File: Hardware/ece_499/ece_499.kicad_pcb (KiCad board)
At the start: 2 copper layers, 110.8 x 70 mm, 63 parts, among them J1 Conn_01x04, J2 Conn_01x04, J3 Conn_01x04, J4 Conn_01x04, J5 Conn_01x04, Q1 DMN2004WK, Q2 DMN2004WK, Q3 DMN2004WK, Q4 DMN2004WK, SW1 Encoder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

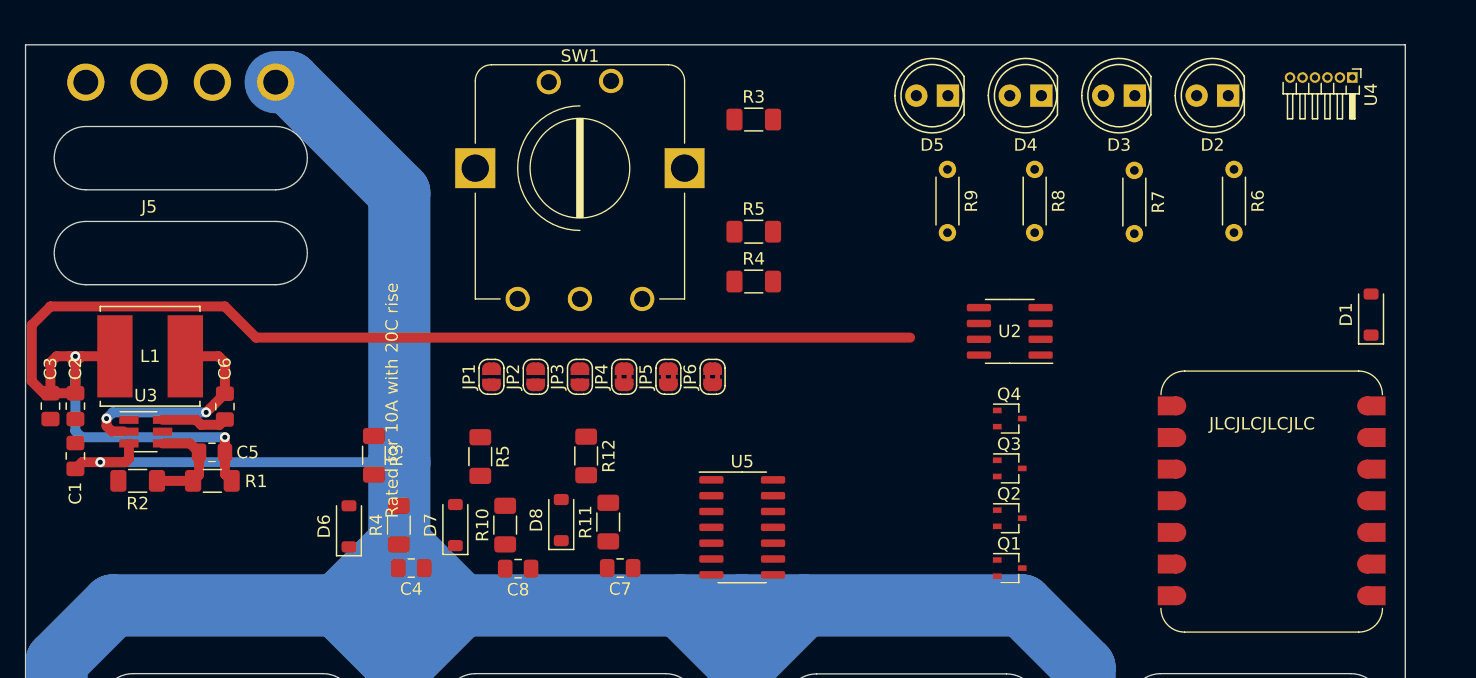
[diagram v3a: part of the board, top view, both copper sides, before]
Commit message: Implement 3v3 lines on PCB
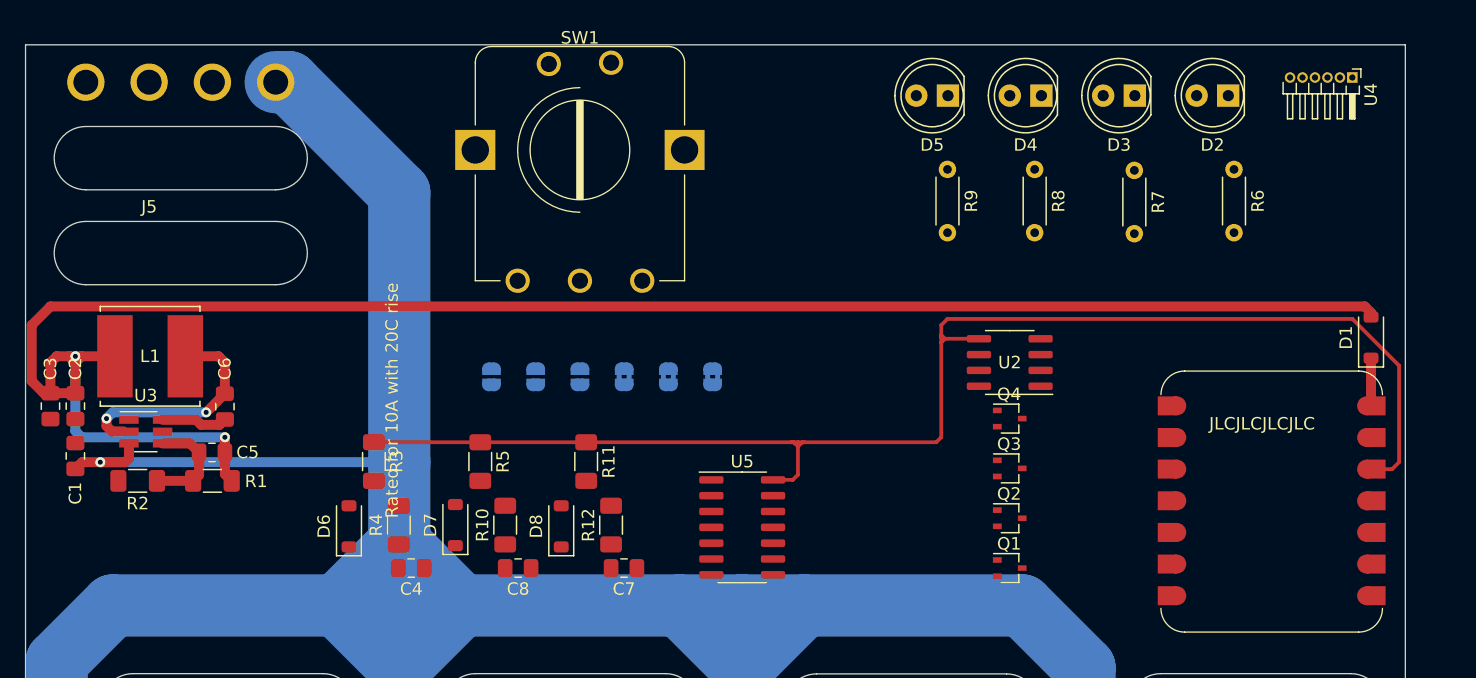
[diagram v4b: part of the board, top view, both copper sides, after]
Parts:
- removed the R3 at (158.4, 36.0)
- removed the R4 at (158.4, 49.0)
- removed the R5 at (158.4, 45.0)
- JP1, JP2, JP3, JP4, JP5, JP6: moved to B.Cu
- moved R12 5.90 mm to (147.0, 68.5), turned to 90 degrees
- moved R11 5.17 mm to (145.0, 63.5), turned to -90 degrees
- moved U2 2.50 mm to (179.0, 55.5)
- moved D1 1.85 mm to (208.0, 53.5)
- moved SW1 1.46 mm to (144.5, 48.9)
- moved D8 0.50 mm to (143.0, 68.7)
- moved R3 0.50 mm to (128.0, 63.5)
- moved R5 0.40 mm to (136.5, 63.5)
- moved C7 0.31 mm to (148.0, 72.0)
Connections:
- U1 pad 10: +3.3V -> +3V3
- U2 pad 5: +3.3V -> +3V3
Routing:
- net +3V3: track 0.00 -> 113.0 mm
- net +5V: track 114.7 -> 151.2 mm
- net Net-(D1-K): track 0.00 -> 4.00 mm

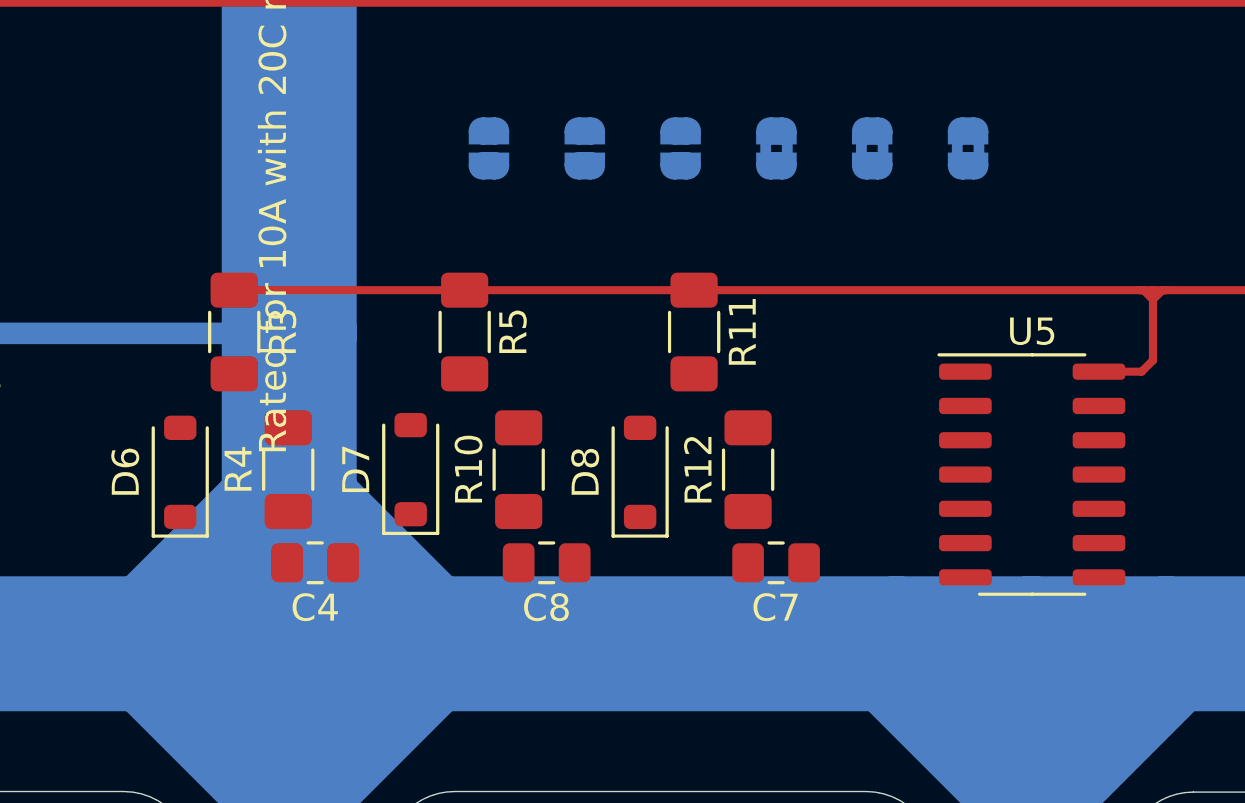
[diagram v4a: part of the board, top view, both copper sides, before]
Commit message: Implement encoder debouncer
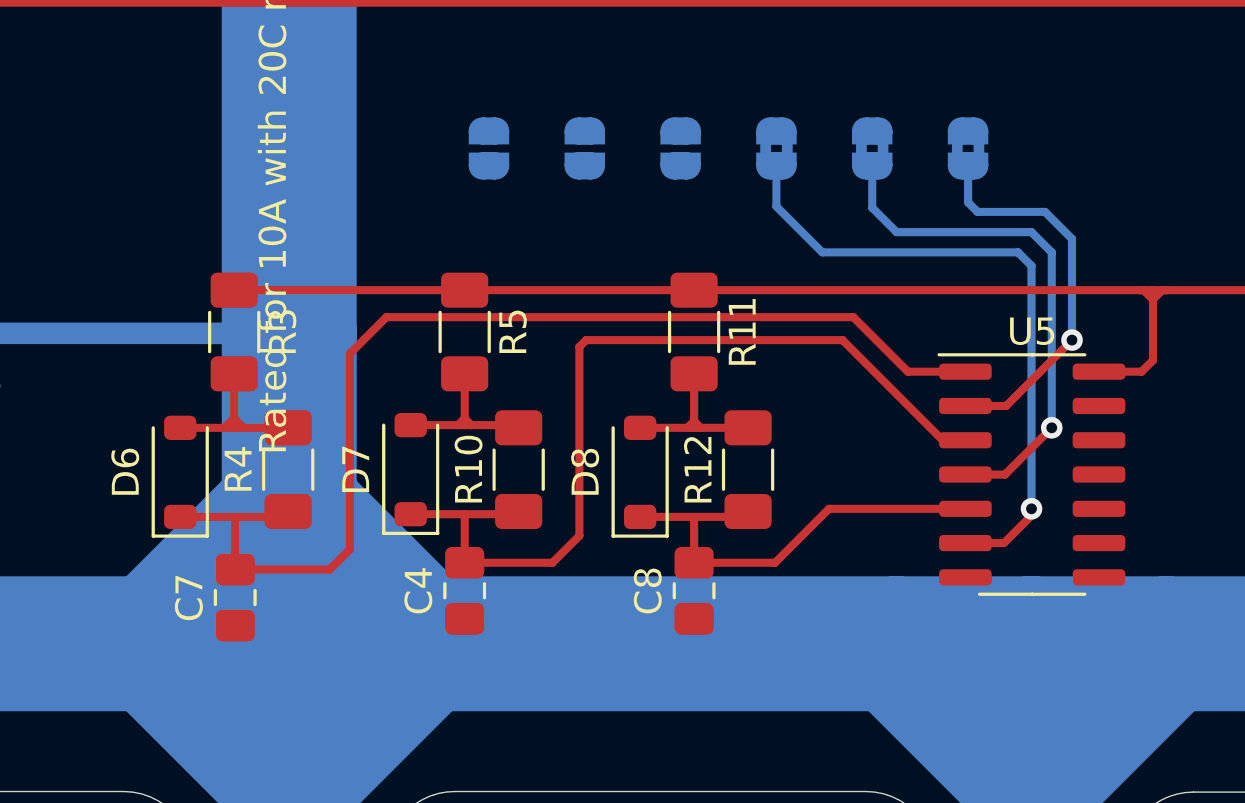
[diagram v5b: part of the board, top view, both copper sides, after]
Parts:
- moved C7 20.1 mm to (128.0, 73.3), turned to 90 degrees
- moved C4 5.63 mm to (136.5, 73.0), turned to 90 degrees
- moved C8 5.56 mm to (145.0, 73.0), turned to 90 degrees
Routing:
- net inverter_1: track 0.00 -> 42.0 mm
- net inverter_2: track 0.00 -> 33.4 mm
- net Net-(JP4-A): track 0.00 -> 24.0 mm, vias 0 -> 1
- net Net-(JP5-A): track 0.00 -> 19.3 mm, vias 0 -> 1
- net Net-(D8-K): track 0.00 -> 16.7 mm
- net Net-(JP6-A): track 0.00 -> 14.5 mm, vias 0 -> 1
- net encoder_sw: track 0.00 -> 7.06 mm
- net encoder_B: track 0.00 -> 6.71 mm
- net encoder_A: track 0.00 -> 6.40 mm

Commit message: Encoder and CAN receiver traces
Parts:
- moved Q1 11.4 mm to (168.0, 69.1)
- moved Q2 11.4 mm to (168.0, 65.1)
- moved JP3 7.75 mm to (136.8, 56.6)
- moved JP1 6.85 mm to (144.2, 56.6)
- moved Q3 6.56 mm to (174.8, 69.0)
- moved Q4 6.56 mm to (174.8, 65.0)
- moved U2 3.34 mm to (179.0, 58.8)
- moved JP2 0.45 mm to (140.5, 56.6)
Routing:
- net controller_sw: track 0.00 -> 98.1 mm, vias 0 -> 4
- net controller_B: track 0.00 -> 89.4 mm, vias 0 -> 4
- net controller_A: track 0.00 -> 84.0 mm, vias 0 -> 4
- net encoder_sw: track 7.06 -> 60.8 mm, vias 0 -> 1
- net Net-(U1-D9): track 0.00 -> 39.0 mm, vias 0 -> 2
- net Net-(U1-D10): track 0.00 -> 38.1 mm, vias 0 -> 2
- net encoder_B: track 6.71 -> 28.2 mm, vias 0 -> 1
- net encoder_A: track 6.40 -> 27.2 mm, vias 0 -> 1
- net +5V: track 151.2 -> 161.6 mm, vias 2 -> 4
- net +3V3: track 113.0 -> 113.5 mm

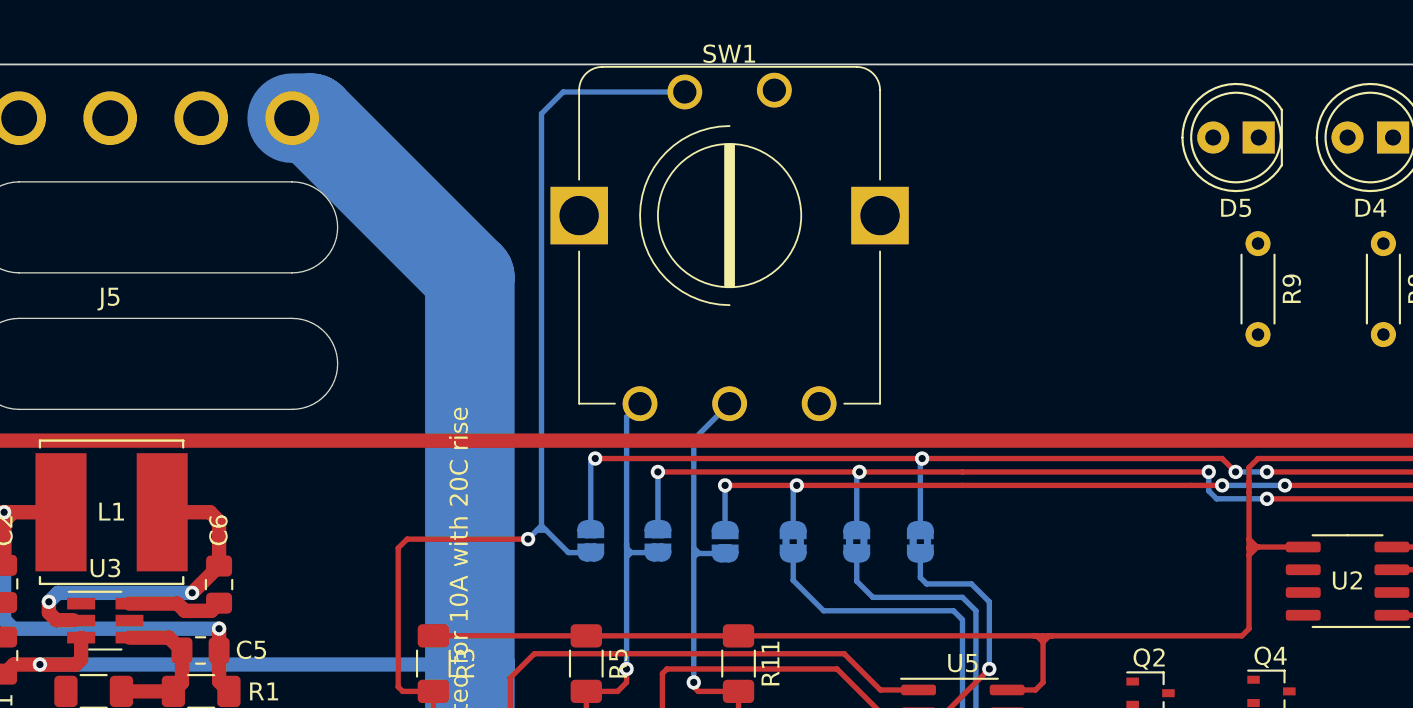
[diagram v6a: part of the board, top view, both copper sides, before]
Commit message: CANBUS tranceiver traces
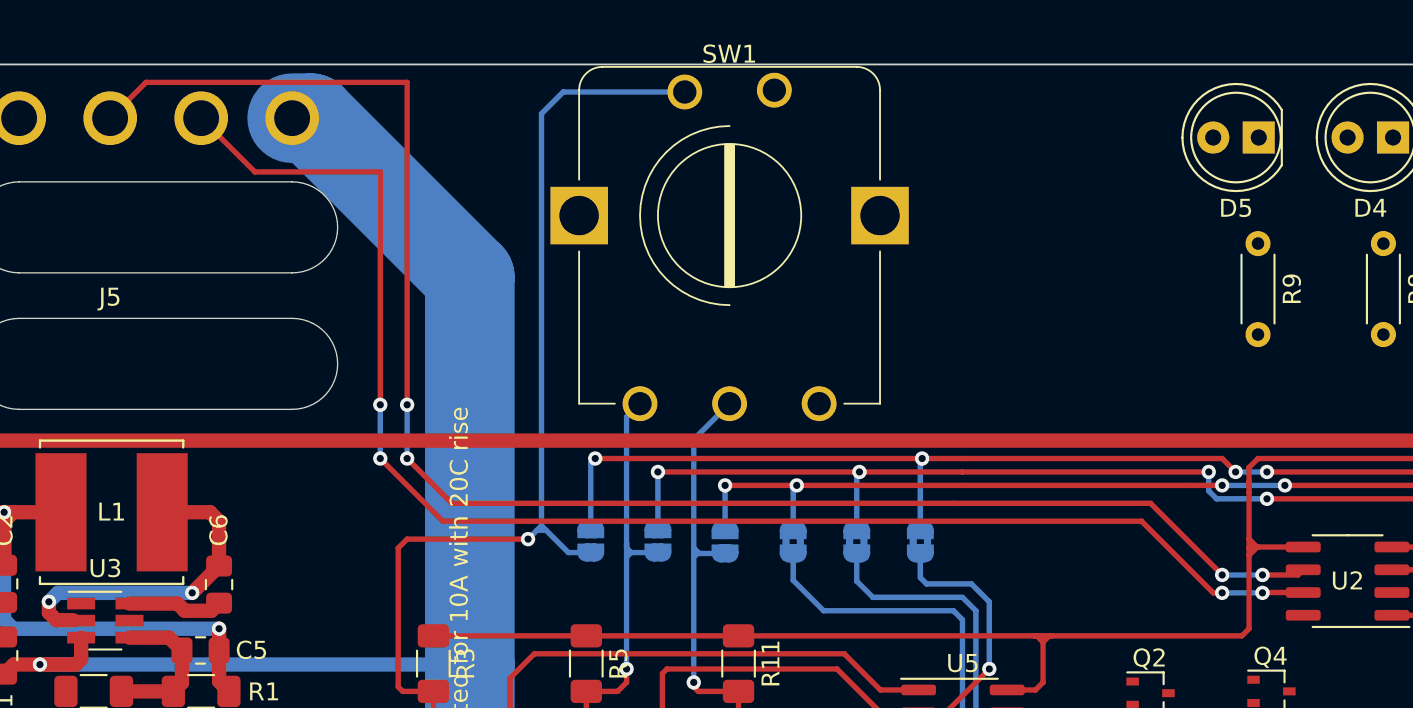
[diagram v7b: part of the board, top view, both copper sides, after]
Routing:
- net Net-(J5-Pin_3): track 0.00 -> 91.2 mm, vias 0 -> 4
- net Net-(J5-Pin_2): track 0.00 -> 81.9 mm, vias 0 -> 4
